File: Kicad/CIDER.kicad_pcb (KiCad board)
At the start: 4 copper layers, 74.9 x 57.1 mm, 63 parts, among them CN1 CDTV-DIAG, J1 JTAG, J2 LED, J3 LED, J4 Conn_02x22_Odd_Even, SW1 SW_DIP_x04, U1 AZ1117-3.3, U10 SST39SF010, U2 XC95144XL-TQ100, U3 74HCT245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

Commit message: PCB: Fixups
* Tweak KEL connector hole sizes
* Fixup MT48LC8M16A2P - Had copied this from the 16M16 part and forgot to make A12 an NC
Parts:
- added C27: 47u, Capacitor_Tantalum_SMD:CP_EIA-3216-18_Kemet-A, F.Cu at (122.5, 104.5)
- RN1: value R_Pack04 -> 10K
- RN2, RN3, RN4, RN5: value R_Pack04 -> 22
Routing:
- net GND: track 76.2 -> 81.3 mm
- net VCC: track 37.6 -> 40.2 mm

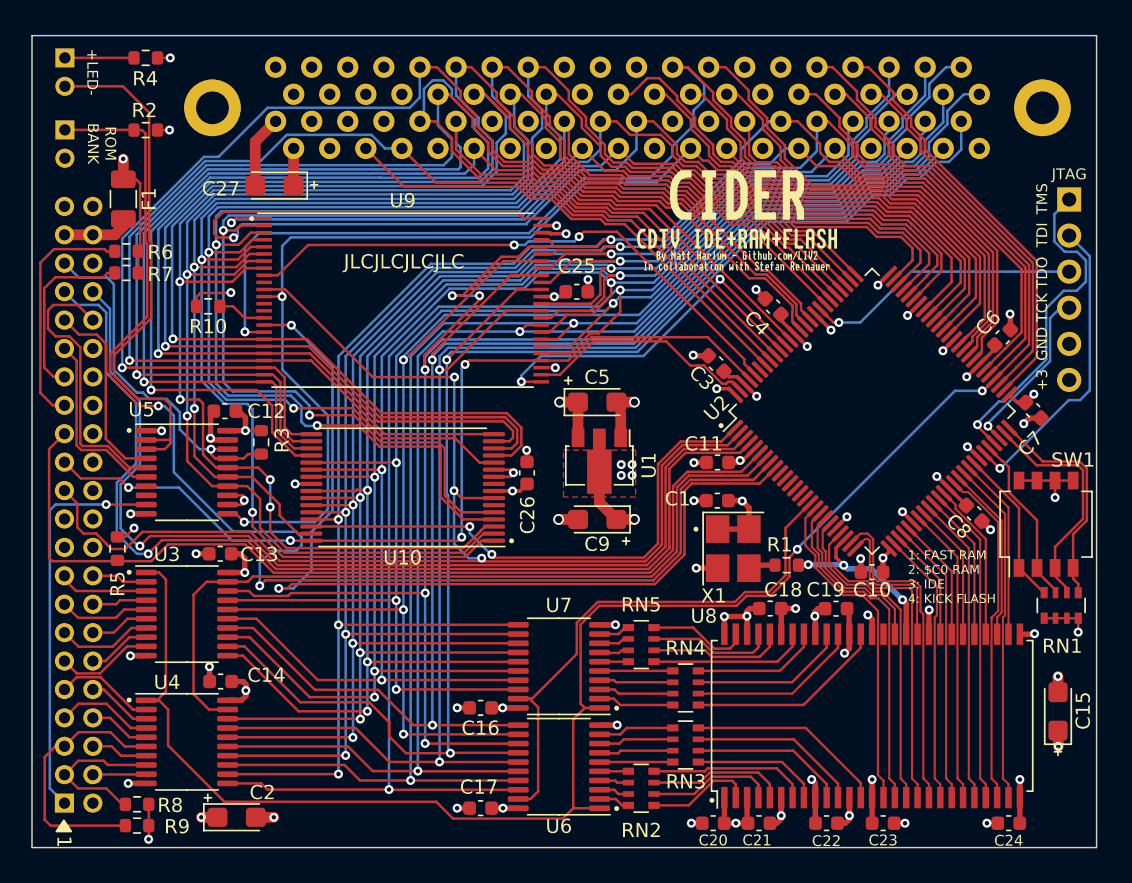
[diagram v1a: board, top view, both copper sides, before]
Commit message: PCB: Connect another CPLD pin to OVR_n
This should give more drive strength to make sure we can drive it low nice and fast
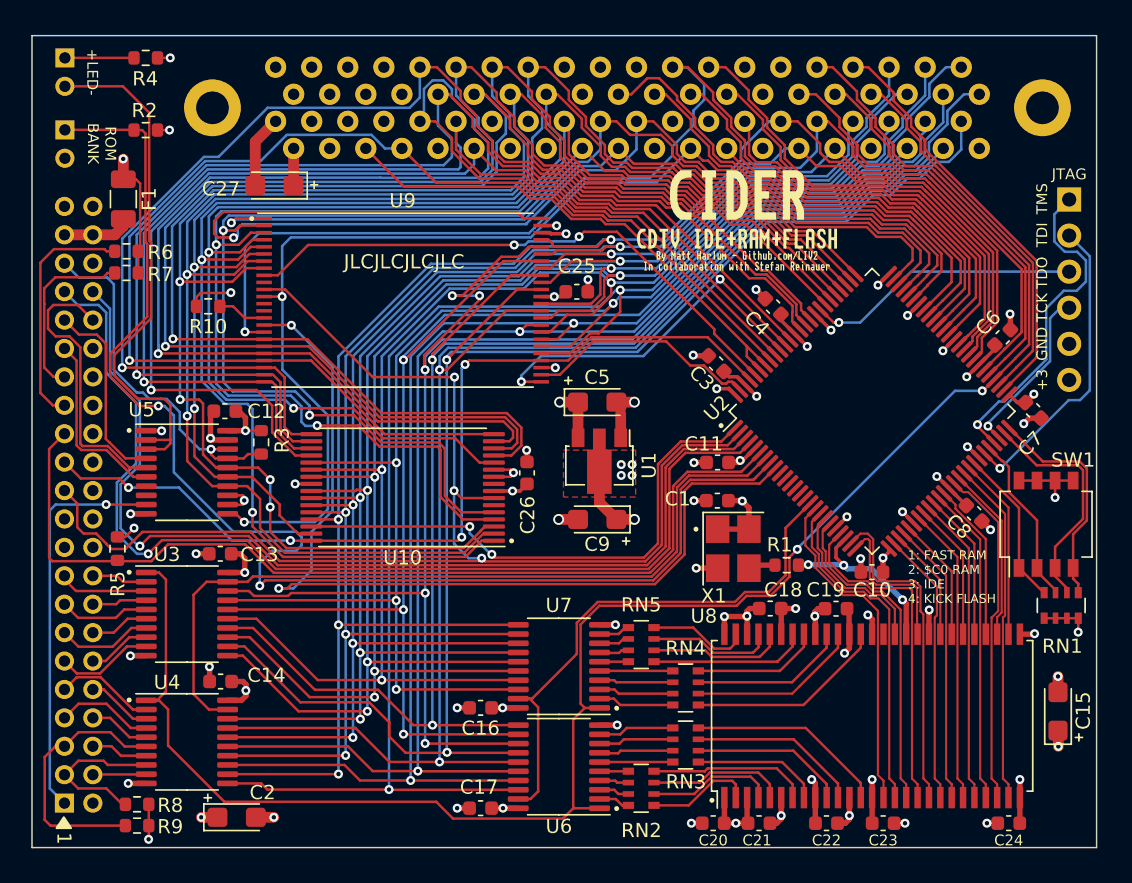
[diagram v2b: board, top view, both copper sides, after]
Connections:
- U2 pad 95: unconnected-(U2-Pad95) -> /Amiga+CPLD/~{OVR}
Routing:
- net /Amiga+CPLD/~{OVR}: track 34.4 -> 36.4 mm

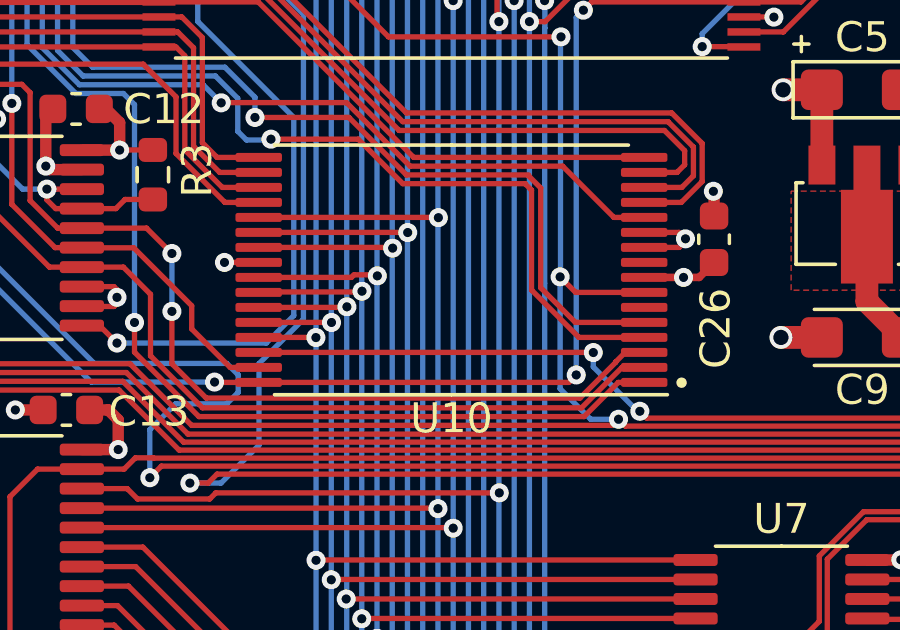
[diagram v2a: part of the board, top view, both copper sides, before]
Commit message: PCB: Connect NC's of 39SF010 to GND
This will allow people to substitute 39SF020/040 if the 010 ever becomes unobtanium
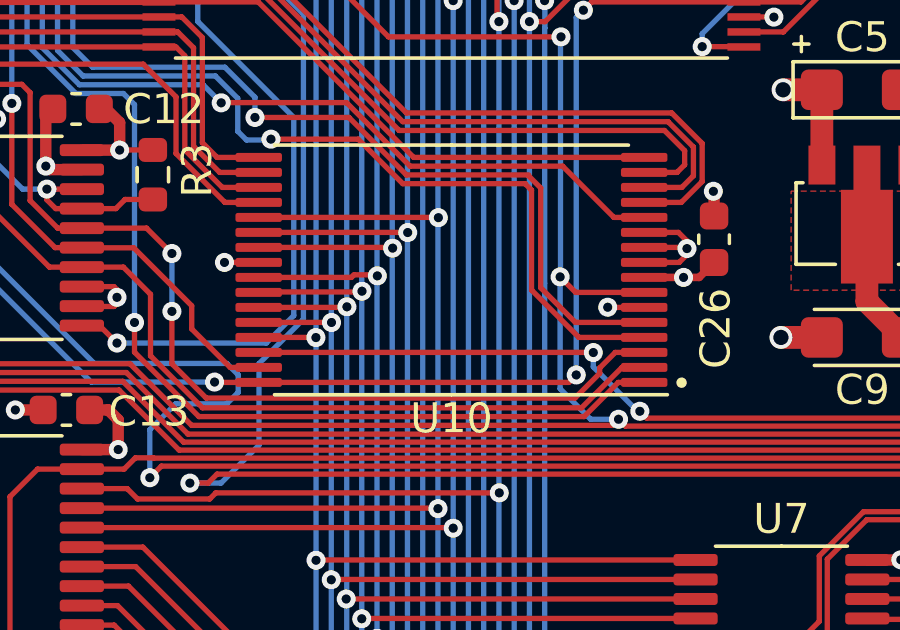
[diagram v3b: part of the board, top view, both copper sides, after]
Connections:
- U10 pad 6: unconnected-(U10-Pad6) -> GND
- U10 pad 9: unconnected-(U10-Pad9) -> GND
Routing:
- net GND: track 81.3 -> 84.5 mm, vias 52 -> 53

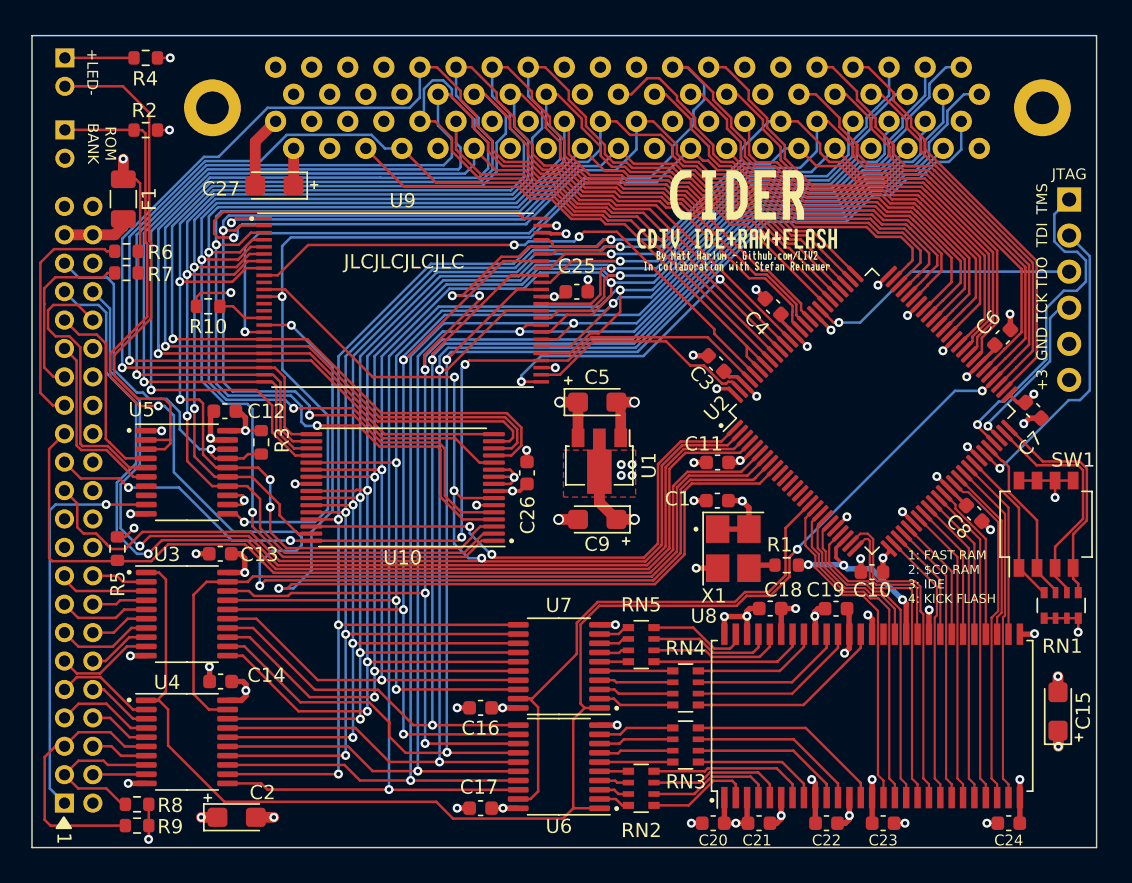
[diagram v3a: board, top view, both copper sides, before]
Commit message: Add ground pours
Apparently JLCPCB are now incapable of producing 4-layer PCBs with less than 30% copper on outer layers...
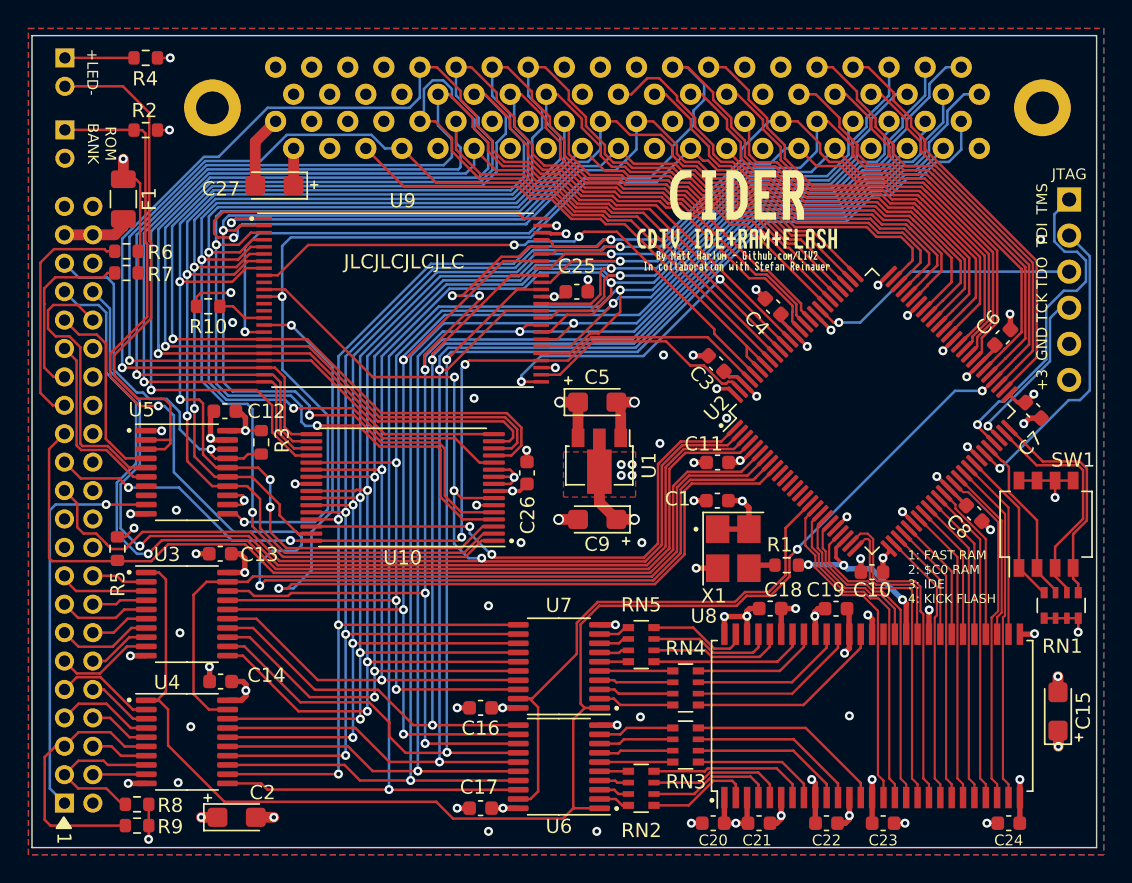
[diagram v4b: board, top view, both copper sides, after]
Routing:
- net GND: vias 53 -> 70
- added copper zone on B.Cu, net GND
- added copper zone on F.Cu, net GND
